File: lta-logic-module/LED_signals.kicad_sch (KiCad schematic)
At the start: 17 parts

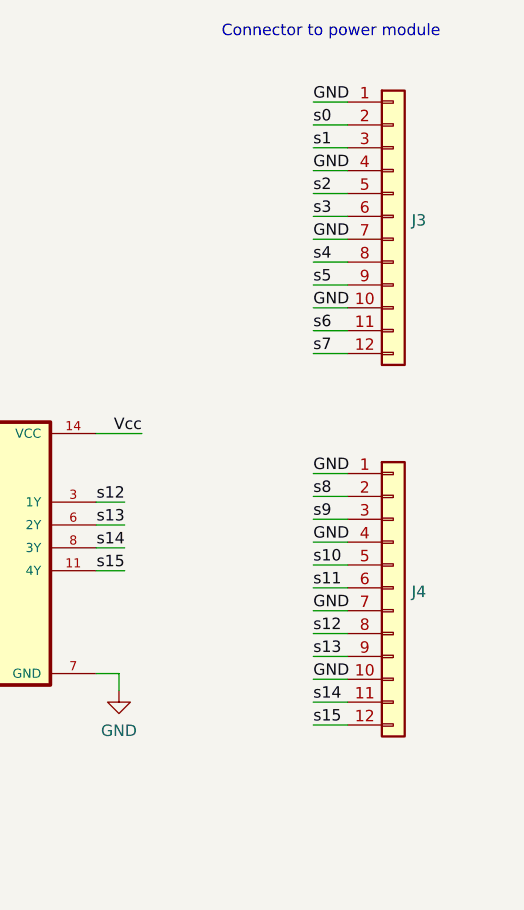
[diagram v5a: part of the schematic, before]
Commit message: Switch 12-pin headers to Molex Micro-Latch c'tors.
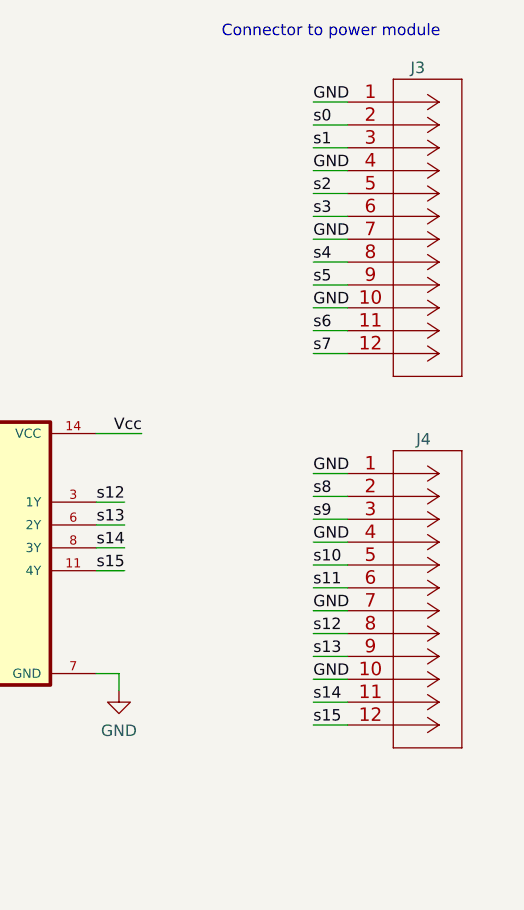
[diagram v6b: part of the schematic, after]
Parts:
- J3, J4: symbol Connector_Generic:Conn_01x12 -> Aaron-Connectors:Molex-MicroLatch-53253-1270; Comment TODO REPLACE FOOTPRINT -> (none); MANUFACTURER (none) -> Molex; MPN XXX TODO FIND -> 532531270
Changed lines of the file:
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@@
     (pin "2")
   )
-  (symbol (lib_id "Connector_Generic:Conn_01x12") (at 269.875 37.465 0) (unit 1)
-    (in_bom yes) (on_board yes) (fields_autoplaced)
-    (property "Reference" "J3" (id 0) (at 271.907 37.9003 0)
-      (effects (font (size 1.27 1.27)) (justify left))
-    )
-    (property "Value" "" (id 1) (at 271.907 40.4372 0)
-      (effects (font (size 1.27 1.27)) (justify left))
-    )
-    (property "Footprint" "" (id 2) (at 269.875 37.465 0)
-      (effects (font (size 1.27 1.27)) hide)
-    )
-    (property "Datasheet" "~" (id 3) (at 269.875 37.465 0)
-      (effects (font (size 1.27 1.27)) hide)
-    )
-    (property "Comment" "TODO REPLACE FOOTPRINT" (id 4) (at 269.875 37.465 0)
-      (effects (font (size 1.27 1.27)) hide)
-    )
-    (property "MPN" "XXX TODO FIND" (id 5) (at 269.875 37.465 0)
+  (symbol (lib_id "Aaron-Connectors:Molex-MicroLatch-53253-1270") (at 264.795 24.765 0) (unit 1)
+    (in_bom yes) (on_board yes)
+    (property "Reference" "J3" (id 0) (at 271.78 20.955 0)
+      (effects (font (size 1.27 1.27)) (justify left))
+    )
+    (property "Value" "" (id 1) (at 251.46 57.15 0)
+      (effects (font (size 1.27 1.27)) (justify left))
+    )
+    (property "Footprint" "" (id 2) (at 273.685 59.055 0)
+      (effects (font (size 1.524 1.524)) hide)
+    )
+    (property "Datasheet" "https://www.molex.com/webdocs/datasheets/pdf/en-us/0532531270_PCB_HEADERS.pdf" (id 3) (at 269.875 15.875 0)
+      (effects (font (size 1.524 1.524)) hide)
+    )
+    (property "Comment" "" (id 4) (at 264.795 24.765 0)
+      (effects (font (size 1.27 1.27)) hide)
+    )
+    (property "MPN" "532531270" (id 5) (at 271.145 13.335 0)
+      (effects (font (size 1.27 1.27)) hide)
+    )
+    (property "MANUFACTURER" "Molex" (id 6) (at 271.145 10.795 0)
       (effects (font (size 1.27 1.27)) hide)
     )
@@
     (pin "1")
   )
-  (symbol (lib_id "Connector_Generic:Conn_01x12") (at 269.875 78.74 0) (unit 1)
-    (in_bom yes) (on_board yes) (fields_autoplaced)
-    (property "Reference" "J4" (id 0) (at 271.907 79.1753 0)
-      (effects (font (size 1.27 1.27)) (justify left))
-    )
-    (property "Value" "" (id 1) (at 271.907 81.7122 0)
-      (effects (font (size 1.27 1.27)) (justify left))
-    )
-    (property "Footprint" "" (id 2) (at 269.875 78.74 0)
-      (effects (font (size 1.27 1.27)) hide)
-    )
-    (property "Datasheet" "~" (id 3) (at 269.875 78.74 0)
-      (effects (font (size 1.27 1.27)) hide)
-    )
-    (property "Comment" "TODO REPLACE FOOTPRINT" (id 4) (at 269.875 78.74 0)
-      (effects (font (size 1.27 1.27)) hide)
-    )
-    (property "MPN" "XXX TODO FIND" (id 5) (at 269.875 78.74 0)
-      (effects (font (size 1.27 1.27)) hide)
-    )
+  (symbol (lib_id "Aaron-Connectors:Molex-MicroLatch-53253-1270") (at 264.795 66.04 0) (unit 1)
+    (in_bom yes) (on_board yes)
+    (property "Reference" "J4" (id 0) (at 272.415 62.23 0)
+      (effects (font (size 1.27 1.27)) (justify left))
+    )
+    (property "Value" "" (id 1) (at 266.065 98.425 0)
+      (effects (font (size 1.524 1.524)))
+    )
+    (property "Footprint" "" (id 2) (at 273.685 100.33 0)
+      (effects (font (size 1.524 1.524)) hide)
+    )
+    (property "Datasheet" "https://www.molex.com/webdocs/datasheets/pdf/en-us/0532531270_PCB_HEADERS.pdf" (id 3) (at 269.875 57.15 0)
+      (effects (font (size 1.524 1.524)) hide)
+    )
+    (property "Comment" "" (id 4) (at 264.795 66.04 0)
+      (effects (font (size 1.27 1.27)) hide)
+    )
+    (property "MPN" "532531270" (id 5) (at 271.145 54.61 0)
+      (effects (font (size 1.27 1.27)) hide)
+    )
+    (property "MANUFACTURER" "Molex" (id 6) (at 271.145 52.07 0)
+      (effects (font (size 1.27 1.27)) hide)
+    )

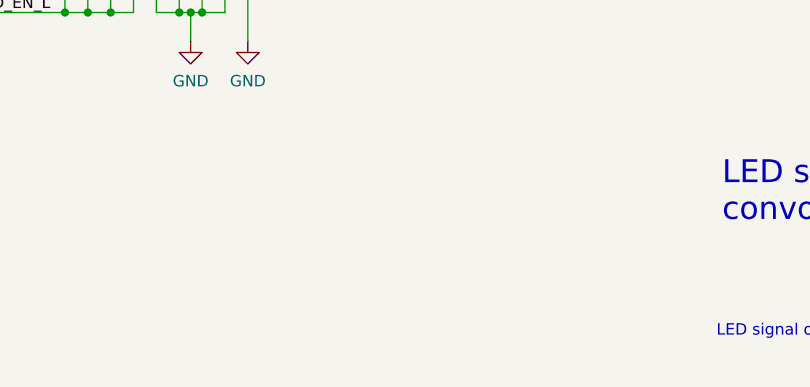
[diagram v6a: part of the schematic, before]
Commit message: Add test points
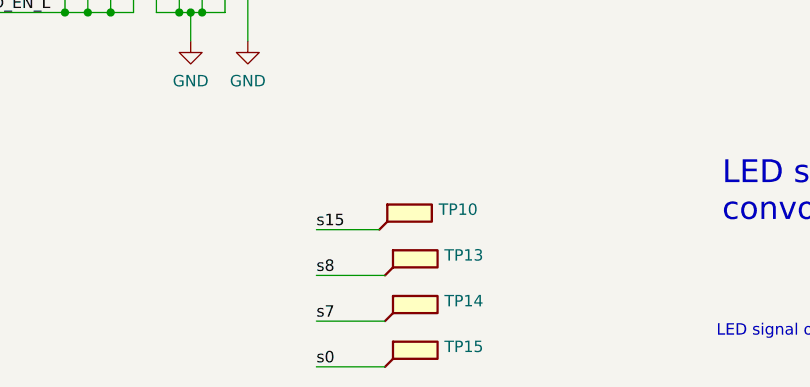
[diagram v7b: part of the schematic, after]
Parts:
- added TP10, TP13, TP14, TP15: (no value), symbol Connector:TestPoint_Flag
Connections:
- net s0: now also TP15.1
- net s15: now also TP10.1
- net s7: now also TP14.1
- net s8: now also TP13.1
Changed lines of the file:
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@@
+    (stroke (width 0) (type default) (color 0 0 0 0))
+  )
+  (wire (pts (xy 146.05 178.435) (xy 153.035 178.435))
     (stroke (width 0) (type default) (color 0 0 0 0))
   )
@@
     (stroke (width 0) (type default) (color 0 0 0 0))
   )
+  (wire (pts (xy 146.05 183.515) (xy 153.67 183.515))
+    (stroke (width 0) (type default) (color 0 0 0 0))
+  )
   (wire (pts (xy 26.035 62.23) (xy 32.385 62.23))
     (stroke (width 0) (type default) (color 0 0 0 0))
@@
     (stroke (width 0) (type default) (color 0 0 0 0))
   )
+  (wire (pts (xy 146.05 188.595) (xy 153.67 188.595))
+    (stroke (width 0) (type default) (color 0 0 0 0))
+  )
   (wire (pts (xy 142.24 88.265) (xy 142.24 90.17))
+    (stroke (width 0) (type default) (color 0 0 0 0))
+  )
+  (wire (pts (xy 146.05 193.675) (xy 153.67 193.675))
     (stroke (width 0) (type default) (color 0 0 0 0))
   )
@@
     (effects (font (size 1.27 1.27)) (justify left bottom))
   )
+  (label "s0" (at 146.05 193.675 0)
+    (effects (font (size 1.27 1.27)) (justify left bottom))
+  )
   (label "Vcc" (at 97.155 61.595 180)
     (effects (font (size 1.27 1.27)) (justify right bottom))
@@
     (effects (font (size 1.27 1.27)) (justify right bottom))
   )
+  (label "s8" (at 146.05 183.515 0)
+    (effects (font (size 1.27 1.27)) (justify left bottom))
+  )
   (label "GND" (at 260.985 40.005 0)
     (effects (font (size 1.27 1.27)) (justify left bottom))
@@
     (effects (font (size 1.27 1.27)) (justify right bottom))
   )
+  (label "s7" (at 146.05 188.595 0)
+    (effects (font (size 1.27 1.27)) (justify left bottom))
+  )
   (label "s9" (at 191.77 71.755 180)
     (effects (font (size 1.27 1.27)) (justify right bottom))
@@
     (effects (font (size 1.27 1.27)) (justify left bottom))
   )
+  (label "s15" (at 146.05 178.435 0)
+    (effects (font (size 1.27 1.27)) (justify left bottom))
+  )
   (label "s7" (at 142.875 76.835 180)
     (effects (font (size 1.27 1.27)) (justify right bottom))
@@
     (pin "1")
     (pin "2")
+  )
+  (symbol (lib_id "Connector:TestPoint_Flag") (at 153.67 188.595 0) (unit 1)
+    (in_bom no) (on_board yes) (fields_autoplaced)
+    (property "Reference" "TP14" (id 0) (at 160.274 186.3633 0)
+      (effects (font (size 1.27 1.27)) (justify left))
+    )
+    (property "Value" "" (id 1) (at 160.274 188.9002 0)
+      (effects (font (size 1.27 1.27)) (justify left))
+    )
+    (property "Footprint" "" (id 2) (at 158.75 188.595 0)
+      (effects (font (size 1.27 1.27)) hide)
+    )
+    (property "Datasheet" "~" (id 3) (at 158.75 188.595 0)
+      (effects (font (size 1.27 1.27)) hide)
+    )
+    (pin "1")
+  )
+  (symbol (lib_id "Connector:TestPoint_Flag") (at 153.67 183.515 0) (unit 1)
+    (in_bom no) (on_board yes) (fields_autoplaced)
+    (property "Reference" "TP13" (id 0) (at 160.274 181.2833 0)
+      (effects (font (size 1.27 1.27)) (justify left))
+    )
+    (property "Value" "" (id 1) (at 160.274 183.8202 0)
+      (effects (font (size 1.27 1.27)) (justify left))
+    )
+    (property "Footprint" "" (id 2) (at 158.75 183.515 0)
+      (effects (font (size 1.27 1.27)) hide)
+    )
+    (property "Datasheet" "~" (id 3) (at 158.75 183.515 0)
+      (effects (font (size 1.27 1.27)) hide)
+    )
+    (pin "1")
+  )
+  (symbol (lib_id "Connector:TestPoint_Flag") (at 153.035 178.435 0) (unit 1)
+    (in_bom no) (on_board yes) (fields_autoplaced)
+    (property "Reference" "TP10" (id 0) (at 159.639 176.2033 0)
+      (effects (font (size 1.27 1.27)) (justify left))
+    )
+    (property "Value" "" (id 1) (at 159.639 178.7402 0)
+      (effects (font (size 1.27 1.27)) (justify left))
+    )
+    (property "Footprint" "" (id 2) (at 158.115 178.435 0)
+      (effects (font (size 1.27 1.27)) hide)
+    )
+    (property "Datasheet" "~" (id 3) (at 158.115 178.435 0)
+      (effects (font (size 1.27 1.27)) hide)
+    )
+    (pin "1")
   )
   (symbol (lib_id "power:GND") (at 191.135 90.17 0) (unit 1)
@@
       (effects (font (size 1.27 1.27)) hide)
     )
+    (pin "1")
+  )
+  (symbol (lib_id "Connector:TestPoint_Flag") (at 153.67 193.675 0) (unit 1)
+    (in_bom no) (on_board yes) (fields_autoplaced)
+    (property "Reference" "TP15" (id 0) (at 160.274 191.4433 0)
+      (effects (font (size 1.27 1.27)) (justify left))
+    )
+    (property "Value" "" (id 1) (at 160.274 193.9802 0)
+      (effects (font (size 1.27 1.27)) (justify left))
+    )
+    (property "Footprint" "" (id 2) (at 158.75 193.675 0)
+      (effects (font (size 1.27 1.27)) hide)
+    )
+    (property "Datasheet" "~" (id 3) (at 158.75 193.675 0)
+      (effects (font (size 1.27 1.27)) hide)
+    )

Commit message: Final tweaks before RTM.
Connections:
- net led12: now also U10.1 (1A); no longer U10.2 (1B)
- net EN0_L renamed EN0
- net EN1_L renamed EN1
- net EN2_L renamed EN2
- net EN3_L renamed EN3
- net EN3: now also U10.2 (1B); no longer U10.1 (1A)
- net LED_EN_L renamed LED_EN
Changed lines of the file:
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@@
     (effects (font (size 1.27 1.27)) (justify left bottom))
   )
-  (label "EN3_L" (at 198.755 80.645 0)
-    (effects (font (size 1.27 1.27)) (justify left bottom))
-  )
-  (label "EN3_L" (at 198.755 65.405 0)
-    (effects (font (size 1.27 1.27)) (justify left bottom))
-  )
-  (label "EN3_L" (at 198.755 75.565 0)
+  (label "EN3" (at 198.755 80.645 0)
+    (effects (font (size 1.27 1.27)) (justify left bottom))
+  )
+  (label "EN3" (at 198.755 67.945 0)
+    (effects (font (size 1.27 1.27)) (justify left bottom))
+  )
+  (label "EN3" (at 198.755 75.565 0)
     (effects (font (size 1.27 1.27)) (justify left bottom))
   )
@@
     (effects (font (size 1.27 1.27)) (justify right bottom))
   )
-  (label "EN1_L" (at 101.6 70.485 0)
+  (label "EN1" (at 101.6 70.485 0)
     (effects (font (size 1.27 1.27)) (justify left bottom))
   )
@@
     (effects (font (size 1.27 1.27)) (justify right bottom))
   )
-  (label "EN0_L" (at 53.975 70.485 0)
+  (label "EN0" (at 53.975 70.485 0)
     (effects (font (size 1.27 1.27)) (justify left bottom))
   )
@@
     (effects (font (size 1.27 1.27)) (justify right bottom))
   )
-  (label "EN1_L" (at 101.6 65.405 0)
+  (label "EN1" (at 101.6 65.405 0)
     (effects (font (size 1.27 1.27)) (justify left bottom))
   )
@@
     (effects (font (size 1.27 1.27)) (justify left bottom))
   )
-  (label "EN2_L" (at 150.495 80.645 0)
+  (label "EN2" (at 150.495 80.645 0)
     (effects (font (size 1.27 1.27)) (justify left bottom))
   )
@@
     (effects (font (size 1.27 1.27)) (justify right bottom))
   )
-  (label "EN2_L" (at 120.65 109.855 270)
+  (label "EN2" (at 120.65 109.855 270)
     (effects (font (size 1.27 1.27)) (justify right bottom))
   )
@@
     (effects (font (size 1.27 1.27)) (justify right bottom))
   )
-  (label "EN2_L" (at 150.495 65.405 0)
+  (label "EN2" (at 150.495 65.405 0)
     (effects (font (size 1.27 1.27)) (justify left bottom))
   )
@@
     (effects (font (size 1.27 1.27)) (justify right bottom))
   )
-  (label "EN2_L" (at 150.495 73.025 0)
+  (label "EN2" (at 150.495 73.025 0)
     (effects (font (size 1.27 1.27)) (justify left bottom))
   )
@@
     (effects (font (size 1.27 1.27)) (justify right bottom))
   )
-  (label "LED_EN_L" (at 107.95 154.305 0)
+  (label "LED_EN" (at 107.95 154.305 0)
     (effects (font (size 1.27 1.27)) (justify left bottom))
   )
@@
     (effects (font (size 1.27 1.27)) (justify left bottom))
   )
-  (label "EN1_L" (at 101.6 75.565 0)
+  (label "EN1" (at 101.6 75.565 0)
     (effects (font (size 1.27 1.27)) (justify left bottom))
   )
@@
     (effects (font (size 1.27 1.27)) (justify right bottom))
   )
-  (label "EN1_L" (at 123.19 109.855 270)
+  (label "EN1" (at 123.19 109.855 270)
     (effects (font (size 1.27 1.27)) (justify right bottom))
   )
@@
     (effects (font (size 1.27 1.27)) (justify left bottom))
   )
-  (label "EN3_L" (at 118.11 109.855 270)
+  (label "EN3" (at 118.11 109.855 270)
     (effects (font (size 1.27 1.27)) (justify right bottom))
   )
@@
     (effects (font (size 1.27 1.27)) (justify left bottom))
   )
-  (label "led12" (at 198.755 67.945 0)
+  (label "led12" (at 198.755 65.405 0)
     (effects (font (size 1.27 1.27)) (justify left bottom))
   )
@@
     (effects (font (size 1.27 1.27)) (justify right bottom))
   )
-  (label "EN1_L" (at 101.6 80.645 0)
+  (label "EN1" (at 101.6 80.645 0)
     (effects (font (size 1.27 1.27)) (justify left bottom))
   )
@@
     (effects (font (size 1.27 1.27)) (justify right bottom))
   )
-  (label "EN0_L" (at 53.975 80.645 0)
+  (label "EN0" (at 53.975 80.645 0)
     (effects (font (size 1.27 1.27)) (justify left bottom))
   )
@@
     (effects (font (size 1.27 1.27)) (justify left bottom))
   )
-  (label "EN0_L" (at 125.73 109.855 270)
+  (label "EN0" (at 125.73 109.855 270)
     (effects (font (size 1.27 1.27)) (justify right bottom))
   )
@@
     (effects (font (size 1.27 1.27)) (justify left bottom))
   )
-  (label "EN0_L" (at 53.975 65.405 0)
+  (label "EN0" (at 53.975 65.405 0)
     (effects (font (size 1.27 1.27)) (justify left bottom))
   )
@@
     (effects (font (size 1.27 1.27)) (justify left bottom))
   )
-  (label "EN0_L" (at 53.975 75.565 0)
-    (effects (font (size 1.27 1.27)) (justify left bottom))
-  )
-  (label "EN2_L" (at 150.495 75.565 0)
+  (label "EN0" (at 53.975 75.565 0)
+    (effects (font (size 1.27 1.27)) (justify left bottom))
+  )
+  (label "EN2" (at 150.495 75.565 0)
     (effects (font (size 1.27 1.27)) (justify left bottom))
   )
@@
     (effects (font (size 1.27 1.27)) (justify right bottom))
   )
-  (label "LED_EN_L" (at 36.83 46.355 180)
+  (label "LED_EN" (at 36.83 46.355 180)
     (effects (font (size 1.27 1.27)) (justify right bottom))
   )
@@
     (effects (font (size 1.27 1.27)) (justify right bottom))
   )
-  (label "EN3_L" (at 198.755 70.485 0)
+  (label "EN3" (at 198.755 70.485 0)
     (effects (font (size 1.27 1.27)) (justify left bottom))
   )
@@
     (effects (font (size 1.27 1.27)) (justify right))
   )
-  (hierarchical_label "LED_EN_L" (shape input) (at 26.035 46.355 180)
-    (effects (font (size 1.27 1.27)) (justify right))
-  )
+  (hierarchical_label "LED_EN" (shape input) (at 26.035 46.355 180)
+    (effects (font (size 1.27 1.27)) (justify right))
+  )
